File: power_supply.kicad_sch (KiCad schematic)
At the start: 14 parts, among them U6 TPS56637, U7 AP2112K-3.3

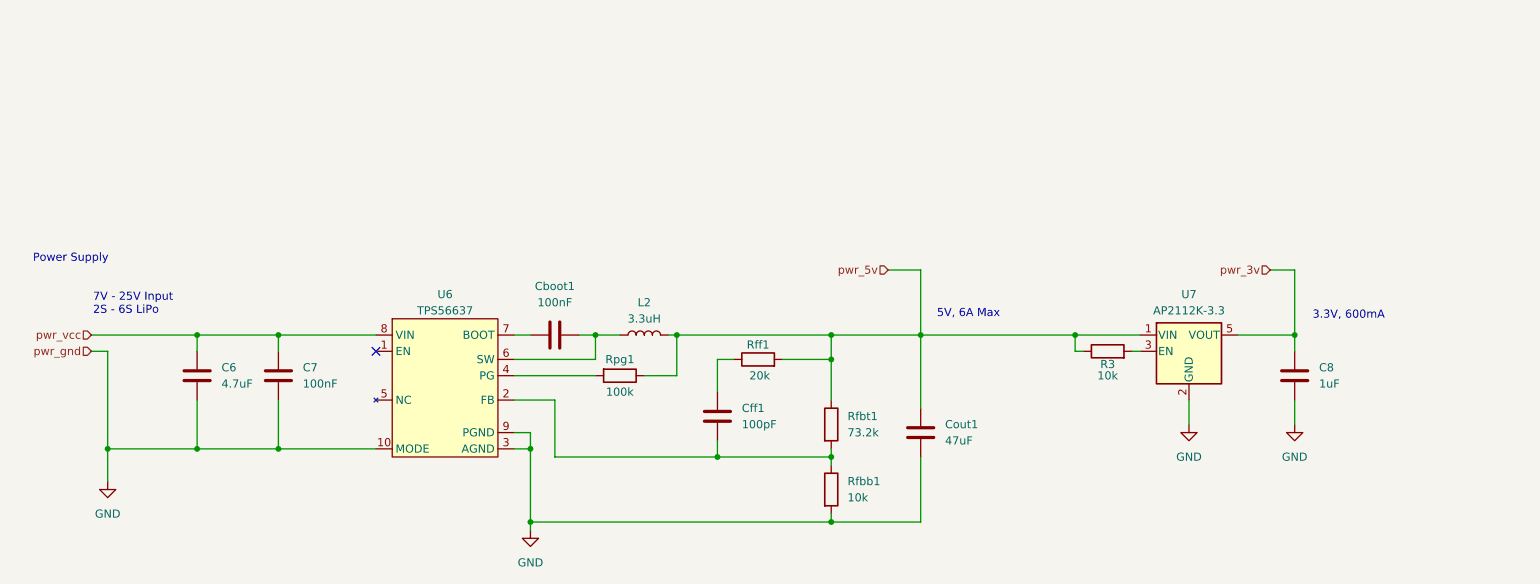
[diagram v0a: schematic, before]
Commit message: Add power supply test points
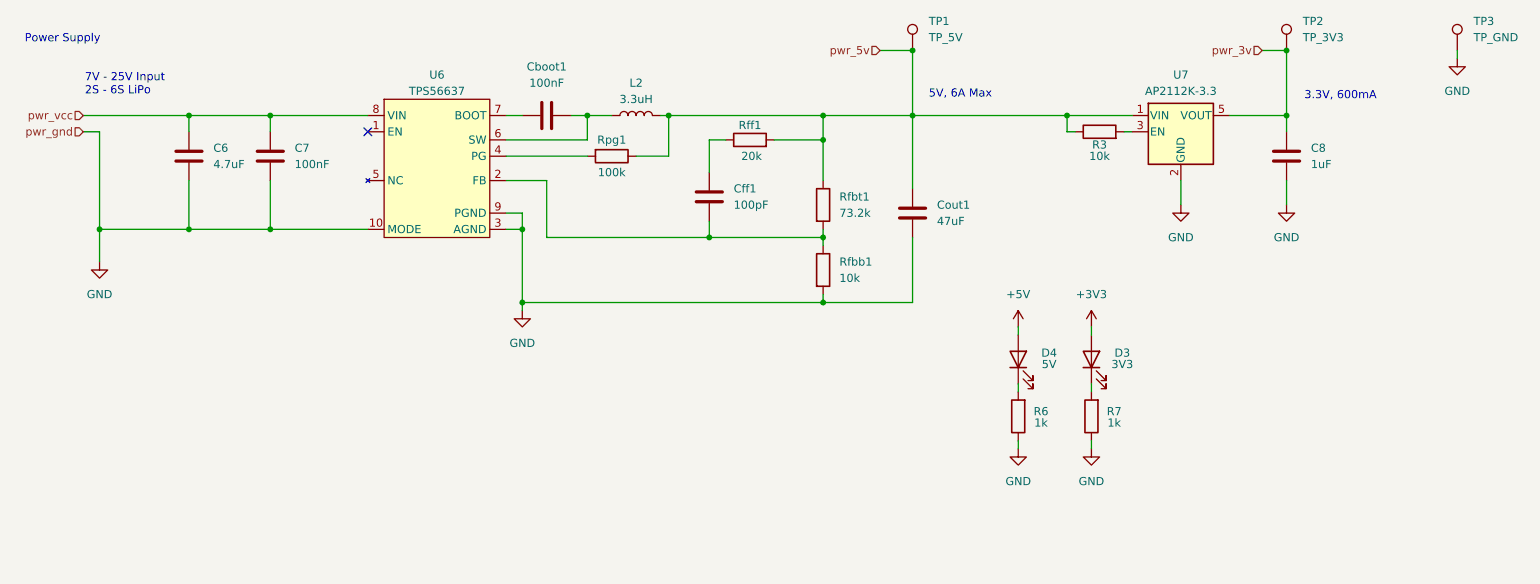
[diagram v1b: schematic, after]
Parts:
- added D3: 3V3, LED_SMD:LED_0603_1608Metric, symbol Device:LED
- added D4: 5V, LED_SMD:LED_0603_1608Metric, symbol Device:LED
- added R6, R7: 1k, Resistor_SMD:R_0402_1005Metric, symbol Device:R
- added TP1: TP_5V, TestPoint:TestPoint_Pad_2.0x2.0mm, symbol Connector:TestPoint
- added TP2: TP_3V3, TestPoint:TestPoint_Pad_2.0x2.0mm, symbol Connector:TestPoint
- added TP3: TP_GND, TestPoint:TestPoint_Pad_2.0x2.0mm, symbol Connector:TestPoint
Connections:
- net GND: now also R6.1, R7.1, TP3.1
- net pwr_3v: now also TP2.1
- net pwr_5v: now also TP1.1
- new net: D3.1 (K), R7.2
- new net: D4.1 (K), R6.2
- new net +3V3: D3.2 (A)
- new net +5V: D4.2 (A)
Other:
- moved on the sheet: C6, C7, C8, Cboot1, Cff1, Cout1, L2, R3, Rfbb1, Rfbt1, Rff1, Rpg1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
